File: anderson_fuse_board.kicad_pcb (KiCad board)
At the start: 2 copper layers, 47 x 105 mm, 13 parts, among them J1 Anderson_two_redblack, J2 Anderson_two_redblack, J3 Anderson_two_redblack, J4 Anderson_two_redblack, J5 Anderson_two_redblack

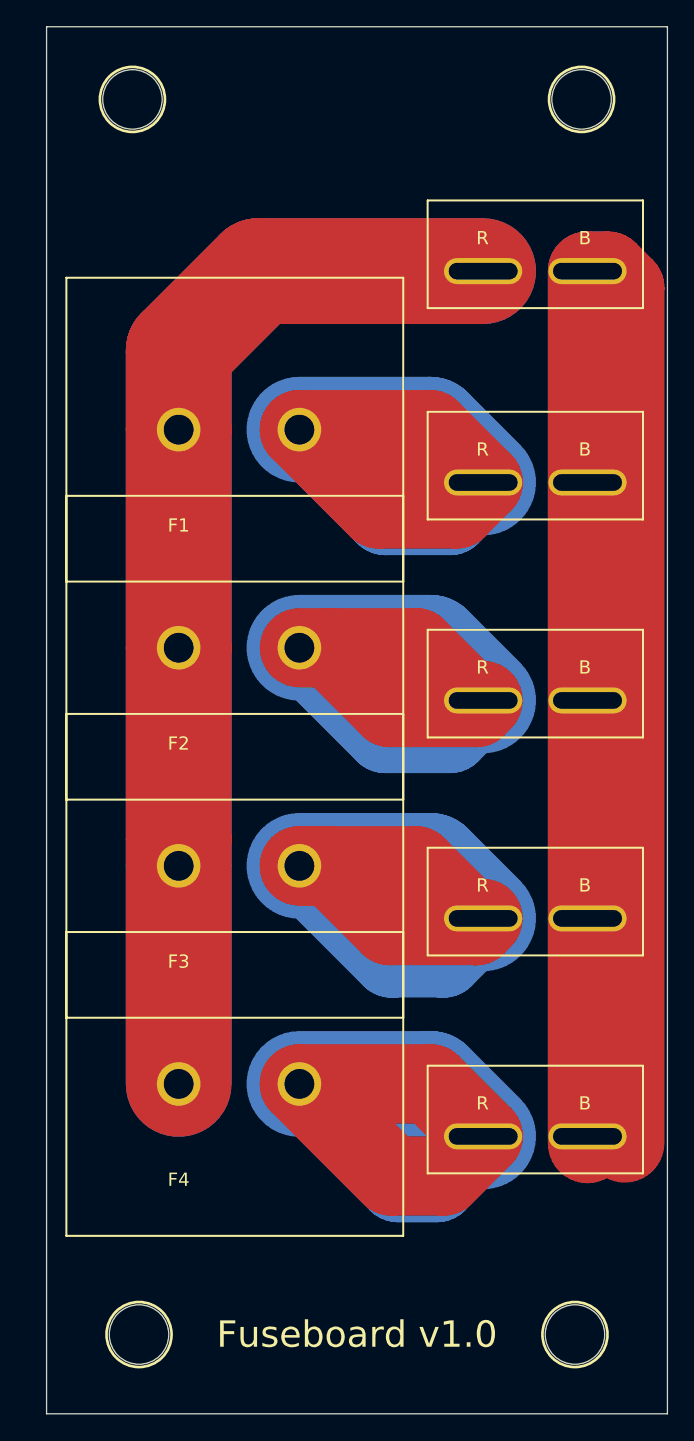
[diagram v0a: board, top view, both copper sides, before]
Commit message: Hardware v1.1:
- Fix silk outline of Anderson connectors
- Switch to standard ATC fuse holder
- Add thermal relief
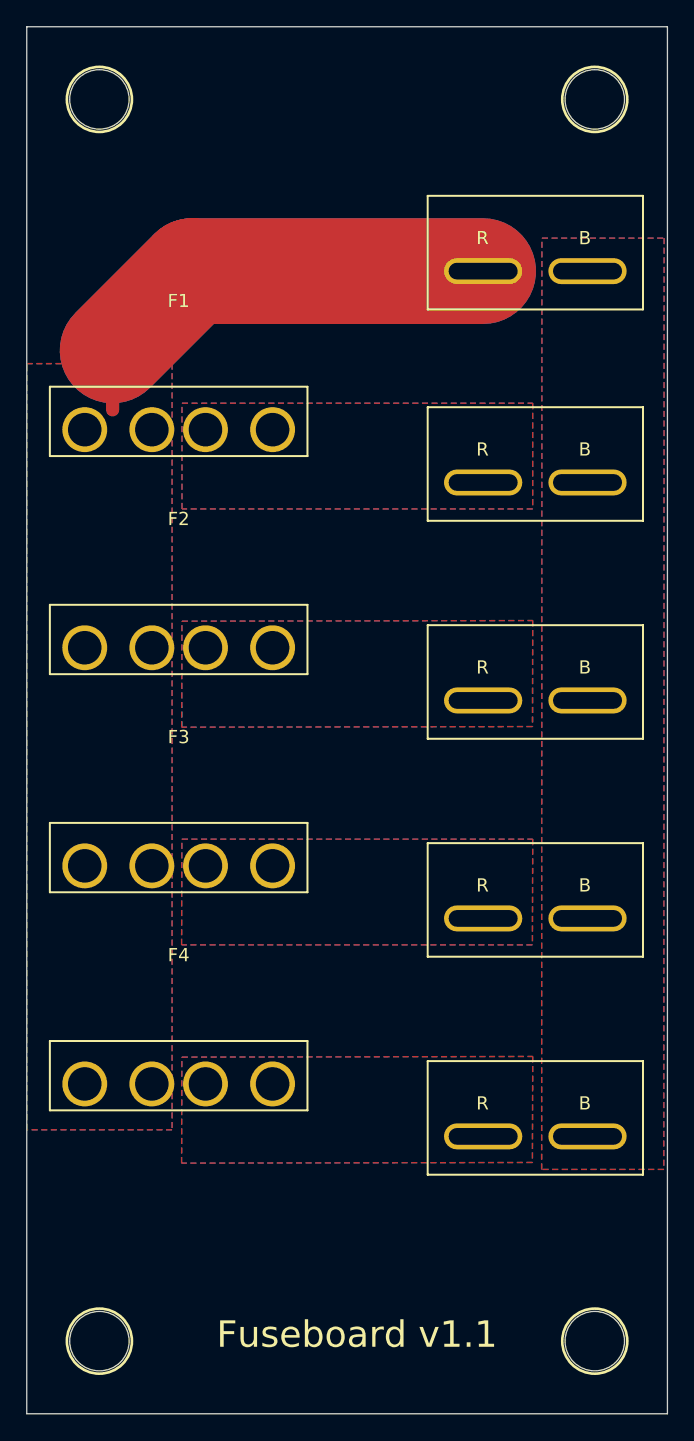
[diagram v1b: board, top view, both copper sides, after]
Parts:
- F1, F2, F3, F4: footprint homebrew:KEYSTONE_3560_ATC_FUSE -> homebrew:FUSEHOLDER_ATC_Bk-6010
- J1, J2, J3, J4, J5: footprint homebrew:Anderson_1337G3_straight_two -> homebrew:Anderson_1335G1_straight_two
- moved H1 3.04 mm to (79.0, 154.0)
- moved H2 2.50 mm to (79.0, 60.0)
- moved H4 1.58 mm to (116.5, 154.0)
- moved H3 1.00 mm to (116.5, 60.0)
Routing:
- net Net-(J1-Pad2): track 266.8 -> 0.00 mm
- net Net-(F1-Pad1): track 162.1 -> 65.6 mm
- net Net-(F4-Pad2): track 67.6 -> 0.00 mm
- net Net-(F1-Pad2): track 66.0 -> 0.00 mm
- net Net-(F3-Pad2): track 64.9 -> 0.00 mm
- net Net-(F2-Pad2): track 62.1 -> 0.00 mm
- added copper zone on B.Cu, net Net-(F1-Pad1)
- added copper zone on F.Cu, net Net-(F1-Pad1)
- added copper zone on B.Cu, net Net-(F1-Pad2)
- added copper zone on F.Cu, net Net-(F1-Pad2)
- added copper zone on B.Cu, net Net-(F2-Pad2)
- added copper zone on F.Cu, net Net-(F2-Pad2)
- added copper zone on B.Cu, net Net-(F3-Pad2)
- added copper zone on F.Cu, net Net-(F3-Pad2)
- added copper zone on B.Cu, net Net-(F4-Pad2)
- added copper zone on F.Cu, net Net-(F4-Pad2)
- added copper zone on B.Cu, net Net-(J1-Pad2)
- added copper zone on F.Cu, net Net-(J1-Pad2)
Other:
- board size 47 x 105 mm -> 48.5 x 105 mm
- board text added: "Fuseboard v1.1"
- board text removed: "Fuseboard v1.0"
